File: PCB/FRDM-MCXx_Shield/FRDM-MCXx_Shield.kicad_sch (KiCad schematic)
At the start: 10 parts, among them J1 Conn_02x08_Odd_Even, J2 Conn_02x06_Odd_Even, J3 Conn_02x10_Odd_Even, J4 Conn_02x08_Odd_Even

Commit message: Updated PCB
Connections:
- net ADC_OUT: no longer J2.2 (Pin_2)
- new net LM35_V_OUT: J2.2 (Pin_2)
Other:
- moved on the sheet: H1, H2
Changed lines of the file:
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@@
 	(title_block
 		(title "Main")
-		(date "2024-04-28")
+		(date "2024-05-05")
 		(rev "V2.0")
 		(company "HAN")
@@
 	(wire
 		(pts
-			(xy 261.62 49.53) (xy 250.19 49.53)
+			(xy 266.7 49.53) (xy 250.19 49.53)
 		)
 		(stroke
@@
 		(exclude_from_sim no)
 		(at 95.25 161.29 0)
-		(size 30.48 31.75)
+		(size 30.48 33.02)
 		(stroke
 			(width 0)
@@
 		)
 	)
-	(text_box "Changes V2.0:\n - Changed pinout.\n - Changed SN74LV164ADR (shftreg) for two 74HC595's. \n \n - Removed extra I2C debug header.\n - Removed FXLS8974CF.\n - Removed buttons.\n - Removed GPS/BT header.\n - Removed RGB-led.\n - Removed Potentiometer.\n\n - Added debug pins.\n - Added test hooks.\n - Added ESD protection diodes.\n"
+	(text_box "Changes V2.0:\n - Changed pinout.\n - Changed SN74LV164ADR (shftreg) for two 74HC595's. \n - Changed ADC_OUT to LM35_V_OUT.\n \n - Removed extra I2C debug header.\n - Removed FXLS8974CF.\n - Removed buttons.\n - Removed GPS/BT header.\n - Removed RGB-led.\n - Removed Potentiometer.\n\n - Added debug pins.\n - Added test hooks.\n - Added ESD protection diodes.\n"
 		(exclude_from_sim no)
 		(at 16.51 161.29 0)
-		(size 59.69 31.75)
+		(size 59.69 33.02)
 		(stroke
 			(width 0)
@@
 		(exclude_from_sim no)
 		(at 135.89 161.29 0)
-		(size 30.48 31.75)
+		(size 30.48 33.02)
 		(stroke
 			(width 0)
@@
 		)
 	)
-	(label "ADC_OUT"
-		(at 261.62 49.53 180)
+	(label "LM35_V_OUT"
+		(at 266.7 49.53 180)
 		(fields_autoplaced yes)
 		(effects
@@
 		)
 	)
-	(label "ADC_OUT"
+	(label "LM35_V_OUT"
 		(at 68.58 71.12 180)
 		(fields_autoplaced yes)
@@
 	(symbol
 		(lib_id "Mechanical:MountingHole")
-		(at 144.78 185.42 0)
+		(at 144.78 187.96 0)
 		(unit 1)
 		(exclude_from_sim yes)
@@
 		(fields_autoplaced yes)
 		(property "Reference" "H2"
-			(at 147.32 184.1499 0)
+			(at 147.32 186.6899 0)
 			(effects
 				(font
@@
 		)
 		(property "Value" "MountingHole"
-			(at 147.32 186.6899 0)
+			(at 147.32 189.2299 0)
 			(effects
 				(font
@@
 		)
 		(property "Footprint" "MountingHole:MountingHole_2.2mm_M2"
-			(at 144.78 185.42 0)
+			(at 144.78 187.96 0)
 			(effects
 				(font
@@
 		)
 		(property "Datasheet" "~"
-			(at 144.78 185.42 0)
+			(at 144.78 187.96 0)
 			(effects
 				(font
@@
 		)
 		(property "Description" "Mounting Hole without connection"
-			(at 144.78 185.42 0)
+			(at 144.78 187.96 0)
 			(effects
 				(font
@@
 	(symbol
 		(lib_id "Mechanical:MountingHole")
-		(at 144.78 170.18 0)
+		(at 144.78 172.72 0)
 		(unit 1)
 		(exclude_from_sim yes)
@@
 		(fields_autoplaced yes)
 		(property "Reference" "H1"
-			(at 147.32 168.9099 0)
+			(at 147.32 171.4499 0)
 			(effects
 				(font
@@
 		)
 		(property "Value" "MountingHole"
-			(at 147.32 171.4499 0)
+			(at 147.32 173.9899 0)
 			(effects
 				(font
@@
 		)
 		(property "Footprint" "MountingHole:MountingHole_2.2mm_M2"
-			(at 144.78 170.18 0)
+			(at 144.78 172.72 0)
 			(effects
 				(font
@@
 		)
 		(property "Datasheet" "~"
-			(at 144.78 170.18 0)
+			(at 144.78 172.72 0)
 			(effects
 				(font
@@
 		)
 		(property "Description" "Mounting Hole without connection"
-			(at 144.78 170.18 0)
+			(at 144.78 172.72 0)
 			(effects
 				(font

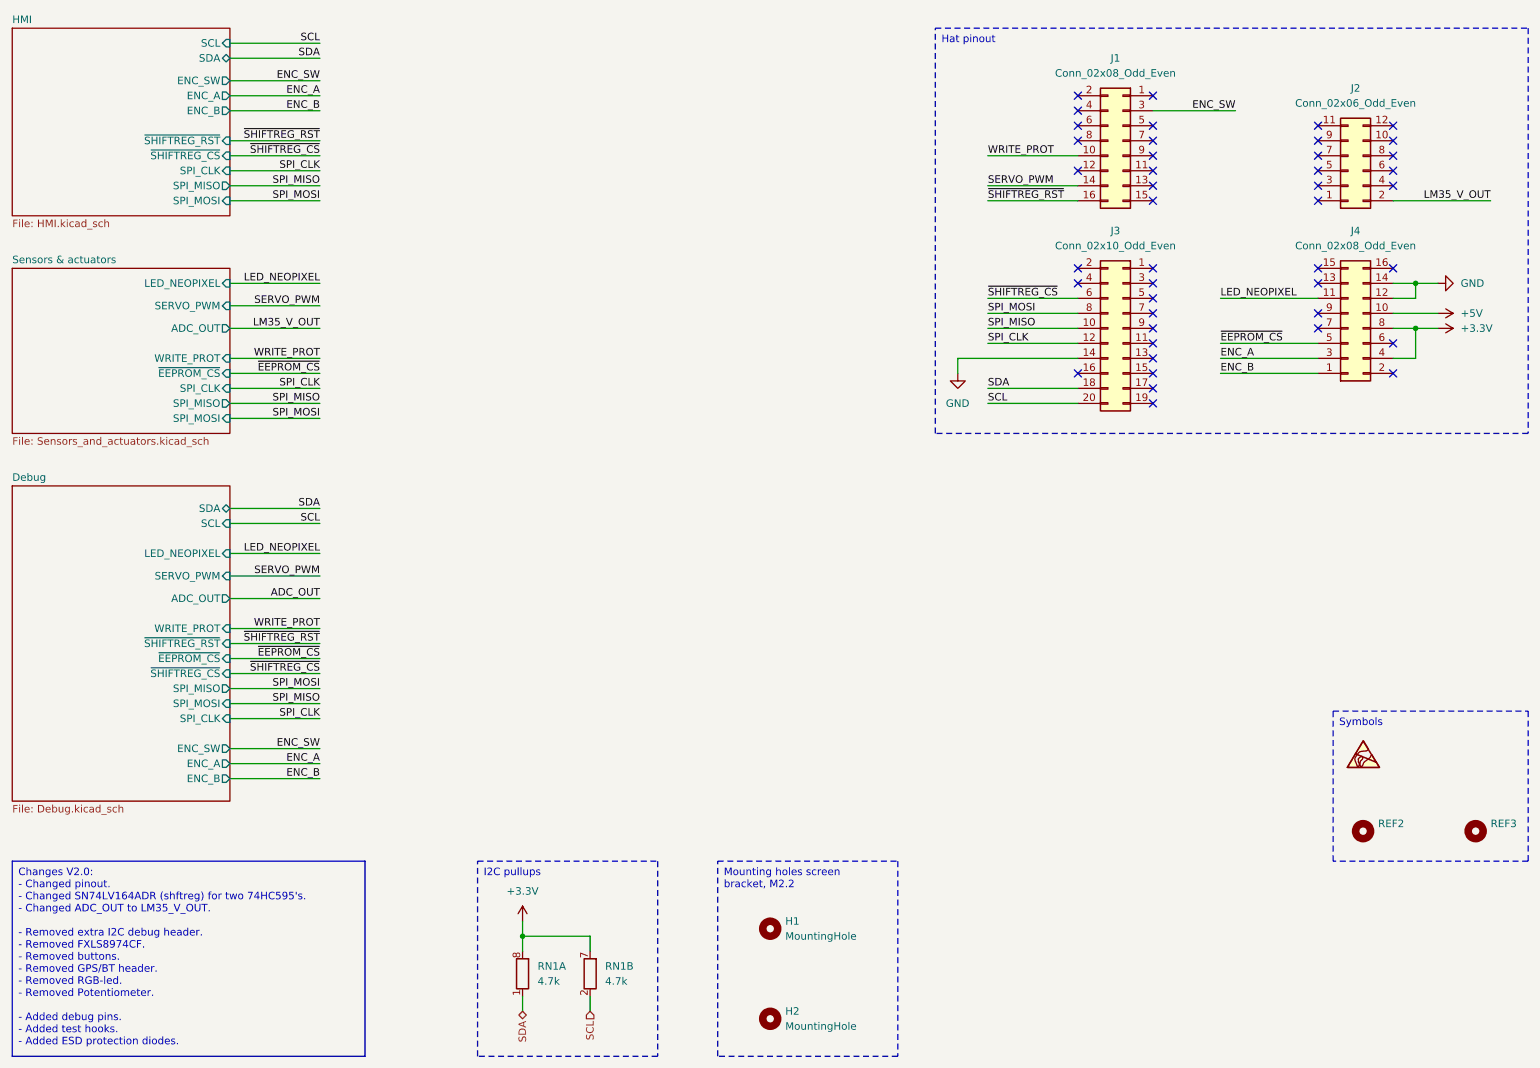
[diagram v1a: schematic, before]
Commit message: Updated labeling and header positions
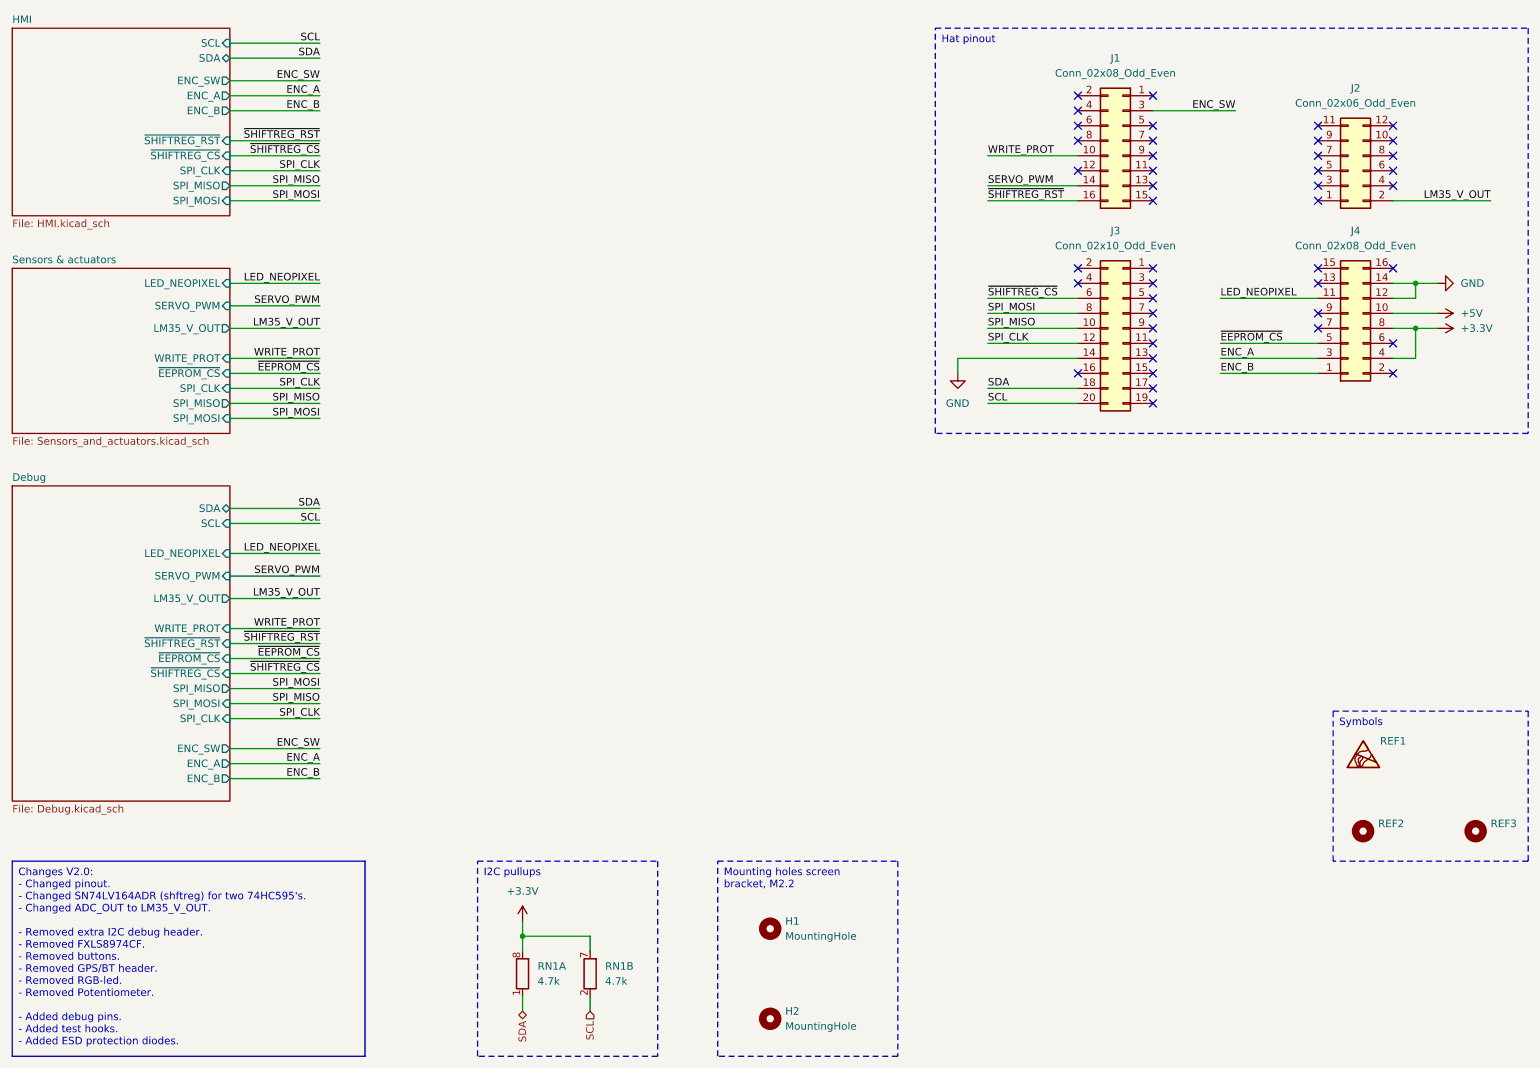
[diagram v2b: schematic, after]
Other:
- sheet Debug ports: added LM35_V_OUT; removed ADC_OUT
- sheet Sensors & actuators ports: added LM35_V_OUT; removed ADC_OUT
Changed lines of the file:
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@@
 	(title_block
 		(title "Main")
-		(date "2024-05-05")
+		(date "2024-05-20")
 		(rev "V2.0")
 		(company "HAN")
@@
 		)
 	)
+	(label "LM35_V_OUT"
+		(at 68.58 116.84 180)
+		(fields_autoplaced yes)
+		(effects
+			(font
+				(size 1.27 1.27)
+			)
+			(justify right bottom)
+		)
+	)
 	(label "SCL"
 		(at 68.58 22.86 180)
@@
 		)
 	)
-	(label "ADC_OUT"
-		(at 68.58 116.84 180)
-		(fields_autoplaced yes)
-		(effects
-			(font
-				(size 1.27 1.27)
-			)
-			(justify right bottom)
-		)
-	)
 	(label "~{SHIFTREG_RST}"
 		(at 68.58 124.46 180)
@@
 		(on_board no)
 		(dnp no)
-		(fields_autoplaced yes)
 		(property "Reference" "REF1"
-			(at 245.11 139.954 0)
+			(at 250.19 140.97 0)
 			(effects
 				(font
 					(size 1.27 1.27)
 				)
-				(hide yes)
 			)
 		)
@@
 			)
 		)
-		(pin "ADC_OUT" output
-			(at 53.34 116.84 0)
-			(effects
-				(font
-					(size 1.27 1.27)
-				)
-				(justify right)
-			)
-		)
 		(pin "SERVO_PWM" input
 			(at 53.34 113.03 0)
@@
 			)
 		)
+		(pin "LM35_V_OUT" output
+			(at 53.34 116.84 0)
+			(effects
+				(font
+					(size 1.27 1.27)
+				)
+				(justify right)
+			)
+		)
 		(instances
 			(project "FRDM-MCXx_Shield"
@@
 			)
 		)
-		(pin "ADC_OUT" output
-			(at 53.34 71.12 0)
-			(effects
-				(font
-					(size 1.27 1.27)
-				)
-				(justify right)
-			)
-		)
 		(pin "WRITE_PROT" input
 			(at 53.34 76.2 0)
@@
 			(effects
 				(font
+					(size 1.27 1.27)
+				)
+				(justify right)
+			)
+		)
+		(pin "LM35_V_OUT" output
+			(at 53.34 71.12 0)
+			(effects
+				(font

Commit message: Added V3
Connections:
- net SCL: now also RN1.1 (R1.1); no longer RN1.2 (R2.1)
- net SDA: now also RN1.2 (R2.1); no longer RN1.1 (R1.1)
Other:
- sheet HMI ports: added none; removed SPI_MISO

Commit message: Updated V3.0
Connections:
- net SERVO_PWM: now also J4.7 (Pin_7); no longer J1.14 (Pin_14)
- net SPI_CLK renamed SPI_SCK
- net WRITE_PROT renamed ~{EEPROM_WP}
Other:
- sheet Debug ports: added SPI_SCK, ~{EEPROM_WP}; removed SPI_CLK, WRITE_PROT
- sheet HMI ports: added SPI_SCK; removed SPI_CLK
- sheet Sensors & actuators ports: added SPI_SCK, ~{EEPROM_WP}; removed SPI_CLK, WRITE_PROT
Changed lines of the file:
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@@
 	(title_block
 		(title "Main")
-		(date "2024-06-13")
+		(date "2024-06-17")
 		(rev "V3.0")
 		(company "HAN")
@@
 	)
 	(no_connect
+		(at 196.85 46.99)
+	)
+	(no_connect
 		(at 196.85 34.29)
 	)
@@
 	)
 	(no_connect
-		(at 237.49 71.12)
-	)
-	(no_connect
 		(at 209.55 76.2)
 	)
@@
 	(wire
 		(pts
-			(xy 196.85 73.66) (xy 181.61 73.66)
+			(xy 237.49 71.12) (xy 222.25 71.12)
 		)
 		(stroke
@@
 	(wire
 		(pts
-			(xy 196.85 46.99) (xy 181.61 46.99)
+			(xy 196.85 73.66) (xy 181.61 73.66)
 		)
 		(stroke
@@
 		)
 	)
-	(text_box "Changes V3.0:\n - Removed capacitor at encoder input.\n - Removed MISO connection with shiftregister.\n \n - Changed 3.3V to 5V at the LM35 power input.  \n - Changed P..... to P....\n"
+	(text_box "Changes V3.0:\n - Removed capacitor at encoder input.\n - Removed MISO connection with shiftregister.\n \n - Changed 3.3V to 5V at the LM35 power input.  \n - Changed P3_12 to P3_10.\n"
 		(exclude_from_sim no)
 		(at 16.51 161.29 0)
@@
 		)
 	)
+	(label "SERVO_PWM"
+		(at 222.25 71.12 0)
+		(fields_autoplaced yes)
+		(effects
+			(font
+				(size 1.27 1.27)
+			)
+			(justify left bottom)
+		)
+	)
 	(label "LED_NEOPIXEL"
 		(at 68.58 106.68 180)
@@
 		)
 	)
-	(label "WRITE_PROT"
-		(at 68.58 119.38 180)
-		(fields_autoplaced yes)
-		(effects
-			(font
-				(size 1.27 1.27)
-			)
-			(justify right bottom)
-		)
-	)
 	(label "ENC_SW"
 		(at 223.52 34.29 180)
@@
 		)
 	)
-	(label "SPI_CLK"
+	(label "SPI_SCK"
 		(at 181.61 73.66 0)
 		(fields_autoplaced yes)
@@
 		)
 	)
-	(label "SPI_CLK"
+	(label "~{EEPROM_WP}"
+		(at 68.58 119.38 180)
+		(fields_autoplaced yes)
+		(effects
+			(font
+				(size 1.27 1.27)
+			)
+			(justify right bottom)
+		)
+	)
+	(label "SPI_SCK"
 		(at 68.58 44.45 180)
 		(fields_autoplaced yes)
@@
 		)
 	)
-	(label "WRITE_PROT"
-		(at 68.58 73.66 180)
-		(fields_autoplaced yes)
-		(effects
-			(font
-				(size 1.27 1.27)
-			)
-			(justify right bottom)
-		)
-	)
 	(label "ENC_A"
 		(at 68.58 31.75 180)
@@
 		)
 	)
-	(label "SERVO_PWM"
-		(at 181.61 46.99 0)
-		(fields_autoplaced yes)
-		(effects
-			(font
-				(size 1.27 1.27)
-			)
-			(justify left bottom)
-		)
-	)
-	(label "SPI_CLK"
+	(label "SPI_SCK"
 		(at 68.58 78.74 180)
 		(fields_autoplaced yes)
@@
 		)
 	)
+	(label "~{EEPROM_WP}"
+		(at 68.58 73.66 180)
+		(fields_autoplaced yes)
+		(effects
+			(font
+				(size 1.27 1.27)
+			)
+			(justify right bottom)
+		)
+	)
 	(label "~{SHIFTREG_RST}"
 		(at 68.58 121.92 180)
@@
 		)
 	)
-	(label "WRITE_PROT"
+	(label "~{EEPROM_WP}"
 		(at 181.61 41.91 0)
 		(fields_autoplaced yes)
@@
 		)
 	)
-	(label "SPI_CLK"
+	(label "SPI_SCK"
 		(at 68.58 134.62 180)
 		(fields_autoplaced yes)
@@
 			)
 		)
-		(pin "SPI_CLK" input
-			(at 53.34 134.62 0)
+		(pin "SPI_MOSI" input
+			(at 53.34 132.08 0)
 			(effects
 				(font
@@
 			)
 		)
-		(pin "SPI_MOSI" input
-			(at 53.34 132.08 0)
+		(pin "~{EEPROM_CS}" input
+			(at 53.34 124.46 0)
 			(effects
 				(font
@@
 			)
 		)
-		(pin "~{EEPROM_CS}" input
-			(at 53.34 124.46 0)
+		(pin "SPI_MISO" output
+			(at 53.34 129.54 0)
 			(effects
 				(font
@@
 			)
 		)
-		(pin "WRITE_PROT" input
-			(at 53.34 119.38 0)
+		(pin "~{SHIFTREG_CS}" input
+			(at 53.34 127 0)
 			(effects
 				(font
@@
 			)
 		)
-		(pin "SPI_MISO" output
-			(at 53.34 129.54 0)
+		(pin "~{SHIFTREG_RST}" input
+			(at 53.34 121.92 0)
 			(effects
 				(font
@@
 			)
 		)
-		(pin "~{SHIFTREG_CS}" input
-			(at 53.34 127 0)
+		(pin "LM35_V_OUT" output
+			(at 53.34 114.3 0)
 			(effects
 				(font
@@
 			)
 		)
-		(pin "~{SHIFTREG_RST}" input
-			(at 53.34 121.92 0)
+		(pin "~{EEPROM_WP}" input
+			(at 53.34 119.38 0)
 			(effects
 				(font
@@
 			)
 		)
-		(pin "LM35_V_OUT" output
-			(at 53.34 114.3 0)
+		(pin "SPI_SCK" input
+			(at 53.34 134.62 0)
 			(effects
 				(font
@@
 			)
 		)
-		(pin "SPI_CLK" input
+		(pin "SPI_SCK" input
 			(at 53.34 44.45 0)
 			(effects
@@
 			)
 		)
-		(pin "WRITE_PROT" input
-			(at 53.34 73.66 0)
+		(pin "~{EEPROM_CS}" input
+			(at 53.34 76.2 0)
 			(effects
 				(font
@@
 			)
 		)
-		(pin "~{EEPROM_CS}" input
-			(at 53.34 76.2 0)
+		(pin "SPI_MOSI" input
+			(at 53.34 83.82 0)
 			(effects
 				(font
@@
 			)
 		)
-		(pin "SPI_CLK" input
-			(at 53.34 78.74 0)
+		(pin "SPI_MISO" output
+			(at 53.34 81.28 0)
 			(effects
 				(font
@@
 			)
 		)
-		(pin "SPI_MOSI" input
-			(at 53.34 83.82 0)
+		(pin "LM35_V_OUT" output
+			(at 53.34 68.58 0)
 			(effects
 				(font
@@
 			)
 		)
-		(pin "SPI_MISO" output
-			(at 53.34 81.28 0)
+		(pin "~{EEPROM_WP}" input
+			(at 53.34 73.66 0)
 			(effects
 				(font
@@
 			)
 		)
-		(pin "LM35_V_OUT" output
-			(at 53.34 68.58 0)
+		(pin "SPI_SCK" input
+			(at 53.34 78.74 0)
 			(effects
 				(font
